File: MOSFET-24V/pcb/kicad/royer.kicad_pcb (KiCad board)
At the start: 2 copper layers, 53.3 x 73.7 mm, 25 parts, among them J1 9-24V, J2 COIL, Q1 IRFB4410, Q2 IRFD110, Q3 IRFD110, Q4 IRFB4410

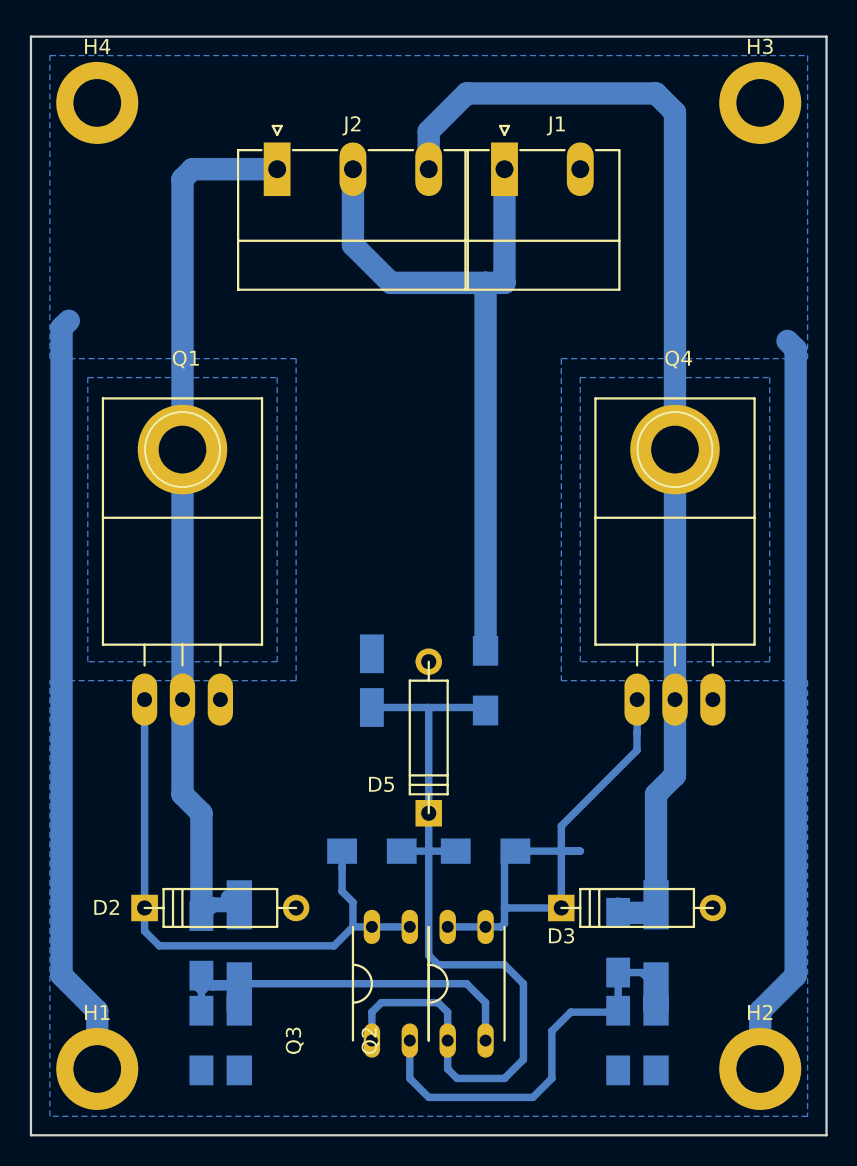
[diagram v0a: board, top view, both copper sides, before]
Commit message: compacting PCB
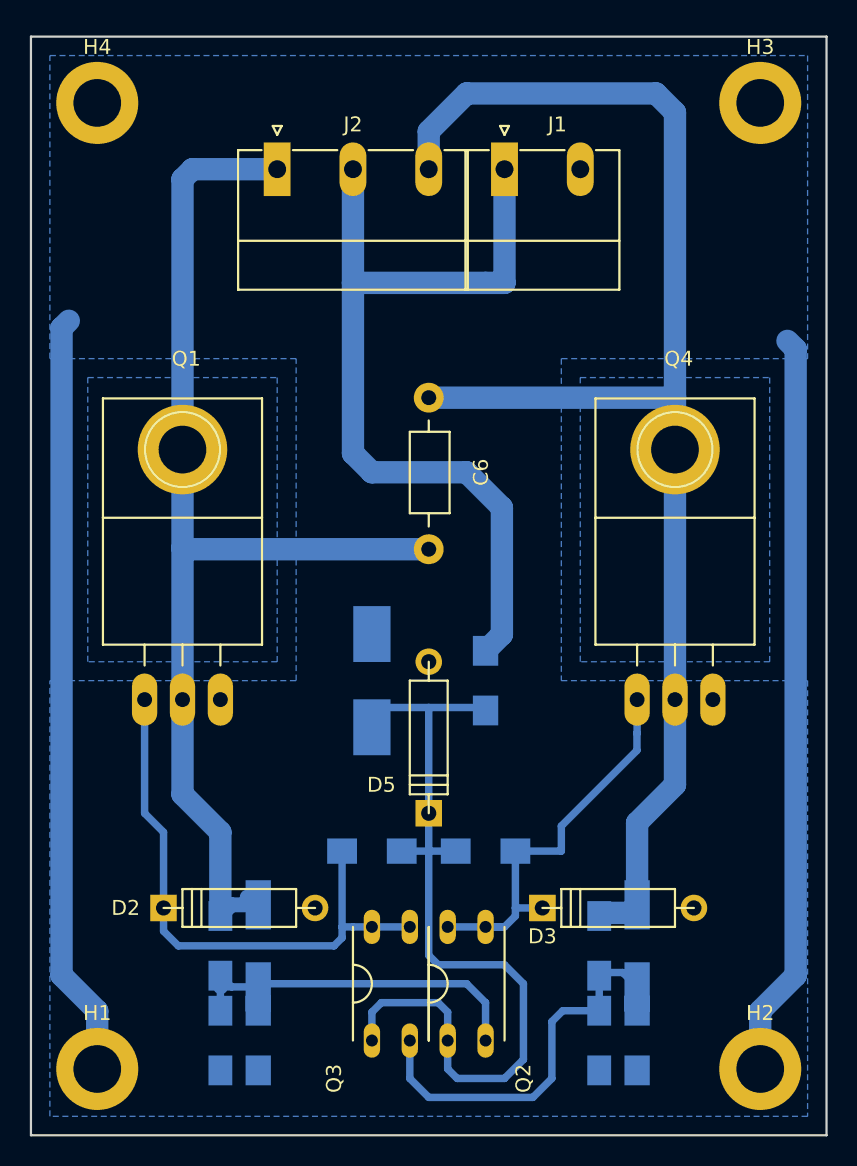
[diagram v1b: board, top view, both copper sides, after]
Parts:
- added C6: 1uF, Choke_Axial_ThroughHole:Choke_Horizontal_RM10mm, F.Cu at (177.8, 99.1)
- C5: value 1uF -> 4.7uF; footprint Capacitors_SMD:c_elec_4x5.8 -> Capacitors_Tantalum_SMD:Tantalum_Case-C_EIA-6032-28_Hand
- moved C4 1.29 mm to (189.2, 130.8)
- moved C1 1.27 mm to (163.8, 130.8)
- moved C2 1.27 mm to (163.8, 137.2)
- moved C3 1.27 mm to (189.2, 137.2)
- moved D1 1.27 mm to (166.4, 130.8)
- moved D3 1.27 mm to (190.5, 128.3)
- moved R1 1.27 mm to (166.4, 137.2)
- moved D2 1.27 mm to (165.1, 128.3)
- moved D4 1.27 mm to (191.8, 130.8)
- moved R5 1.27 mm to (191.8, 137.2)
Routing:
- net /C1: track 59.6 -> 77.4 mm
- net /C2: track 78.1 -> 94.4 mm
- net /24V: track 48.6 -> 58.4 mm
- net /G2: track 34.3 -> 27.4 mm
- net /D1: track 28.2 -> 24.4 mm
- net /D2: track 29.9 -> 29.1 mm
- net /G1: track 41.3 -> 40.7 mm

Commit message: compacting PCB
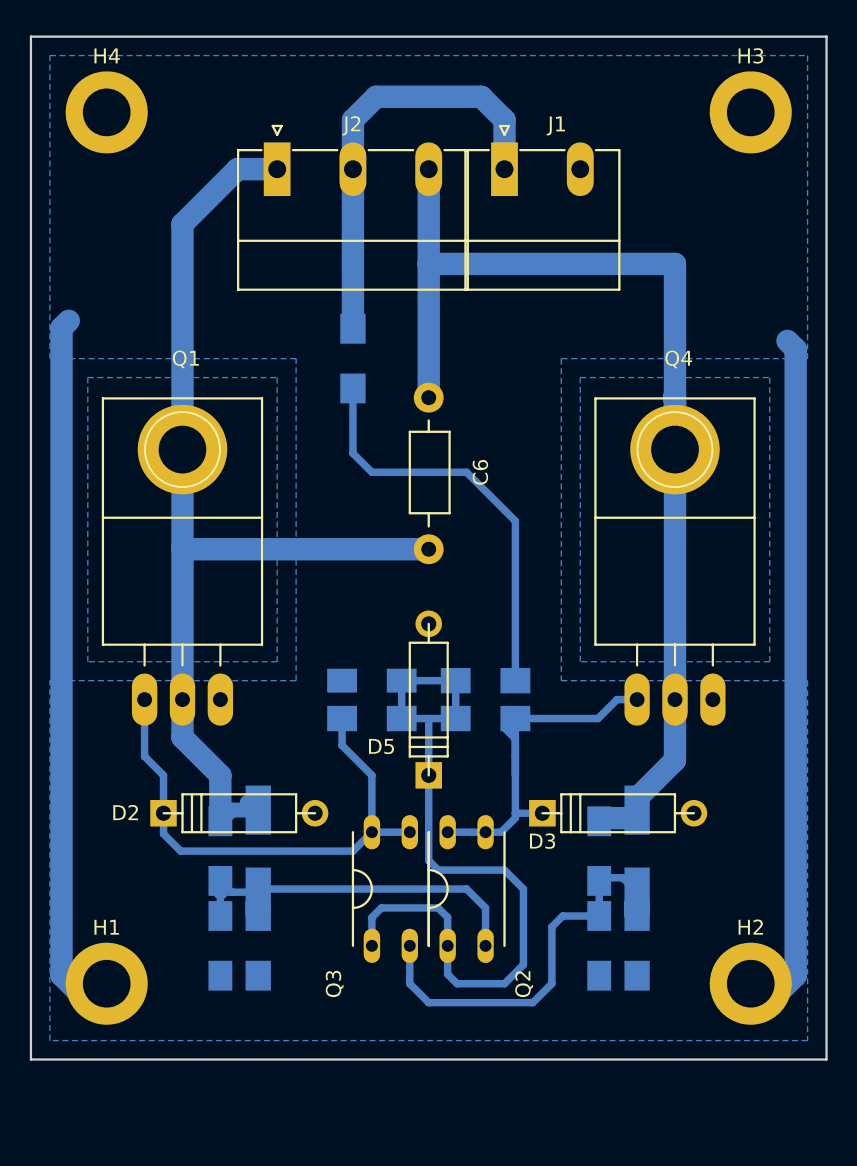
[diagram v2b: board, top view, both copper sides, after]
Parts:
- removed R7: 1.5k, Resistors_SMD:R_1206_HandSoldering
- added R2: 47k, Resistors_SMD:R_1206_HandSoldering, B.Cu at (181.6, 115.6)
- added R6: 1k, Resistors_SMD:R_1206_HandSoldering, B.Cu at (172.7, 91.4)
- C5: value 4.7uF -> 47nF; footprint Capacitors_Tantalum_SMD:Tantalum_Case-C_EIA-6032-28_Hand -> Capacitors_SMD:C_1206_HandSoldering
- R4: value 47k -> 33k
- R5: value 33k -> 1k
- moved R5 26.2 mm to (181.6, 113.0), turned to 180 degrees
- moved R4 18.9 mm to (191.8, 130.8), turned to 270 degrees
- moved R3 11.7 mm to (174.0, 115.6), turned to 180 degrees
- moved C1 6.35 mm to (163.8, 124.5)
- moved C4 6.35 mm to (189.2, 124.5)
- moved D1 6.35 mm to (166.4, 124.5)
- moved D2 6.35 mm to (165.1, 121.9)
- moved D3 6.35 mm to (190.5, 121.9)
- moved D4 6.35 mm to (191.8, 124.5)
- moved C2 6.35 mm to (163.8, 130.8)
- moved C3 6.35 mm to (189.2, 130.8)
- moved Q2 6.35 mm to (179.1, 130.8)
- moved Q3 6.35 mm to (174.0, 130.8)
- moved R1 6.35 mm to (166.4, 130.8)
- moved H1 5.75 mm to (156.2, 133.3)
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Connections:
- R3 pad 2: /G2 -> /G1
- R4 pad 1: /9V -> /D2
- R4 pad 2: /G1 -> GND
- R5 pad 1: /D2 -> Net-(R5-Pad1)
- R5 pad 2: GND -> /9V
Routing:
- net /24V: track 58.4 -> 28.8 mm
- net Net-(R5-Pad1): track 0.00 -> 27.8 mm
- net /C2: track 94.4 -> 76.2 mm
- net /C1: track 77.4 -> 69.3 mm
- net GND: track 101.4 -> 93.6 mm
- net /9V: track 57.3 -> 51.3 mm
- net /G1: track 40.7 -> 35.5 mm
- net /G2: track 27.4 -> 25.6 mm
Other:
- board size 53.3 x 73.7 mm -> 53.3 x 68.6 mm

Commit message: enlarging holes 3.2->3.5 mm# Please enter the commit message for your changes. Lines starting
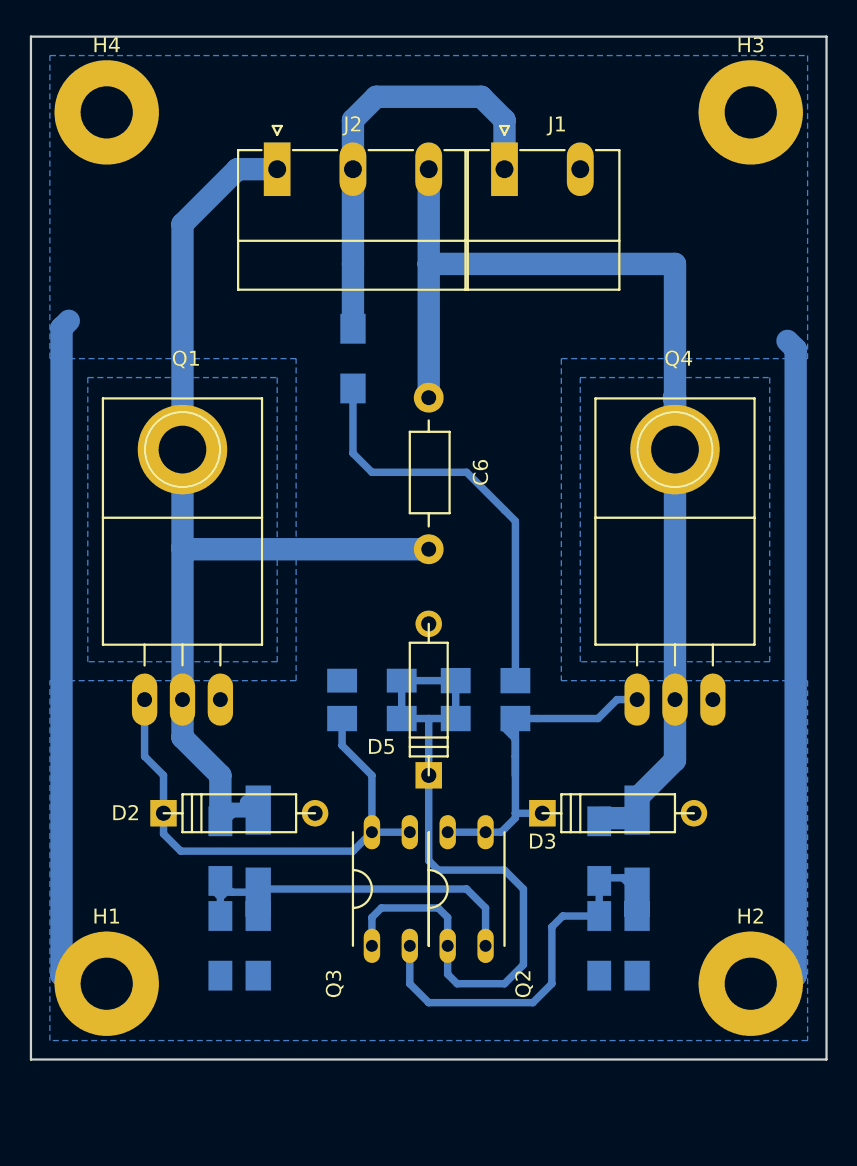
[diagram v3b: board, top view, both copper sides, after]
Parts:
- H1, H2, H3, H4: value 3.2mm -> 3.5mm; footprint Mounting_Holes:MountingHole_3.2mm_M3_ISO14580_Pad -> Mounting_Holes:MountingHole_3.5mm_Pad
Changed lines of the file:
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@@
     )
-  )
-  (module Mounting_Holes:MountingHole_3.2mm_M3_ISO14580_Pad (layer F.Cu)
-    (at 156.21 133.35)
-    (descr "Mounting Hole 3.2mm, M3, ISO14580")
-    (tags "mounting hole 3.2mm m3 iso14580")
-    (fp_text reference H1 (at 0 -3.75) (layer F.SilkS)
-      (effects (font (size 1 1) (thickness 0.15)))
-    )
-    (fp_text value 3.2mm (at 0 3.75) (layer F.Fab)
-      (effects (font (size 1 1) (thickness 0.15)))
-    )
-    (fp_circle (center 0 0) (end 2.75 0) (layer Cmts.User) (width 0.15))
-    (fp_circle (center 0 0) (end 3 0) (layer F.CrtYd) (width 0.05))
-    (pad 1 thru_hole circle (at 0 0) (size 5.5 5.5) (drill 3.2) (layers *.Cu *.Mask)
-      (net 1 GND))
-  )
-  (module Mounting_Holes:MountingHole_3.2mm_M3_ISO14580_Pad (layer F.Cu)
-    (at 199.39 133.35)
-    (descr "Mounting Hole 3.2mm, M3, ISO14580")
-    (tags "mounting hole 3.2mm m3 iso14580")
-    (fp_text reference H2 (at 0 -3.75) (layer F.SilkS)
-      (effects (font (size 1 1) (thickness 0.15)))
-    )
-    (fp_text value 3.2mm (at 0 3.75) (layer F.Fab)
-      (effects (font (size 1 1) (thickness 0.15)))
-    )
-    (fp_circle (center 0 0) (end 2.75 0) (layer Cmts.User) (width 0.15))
-    (fp_circle (center 0 0) (end 3 0) (layer F.CrtYd) (width 0.05))
-    (pad 1 thru_hole circle (at 0 0) (size 5.5 5.5) (drill 3.2) (layers *.Cu *.Mask)
-      (net 1 GND))
   )
   (module TO-220:TO-220_Neutral123_Horizontal_LargePads (layer F.Cu)
@@
     )
   )
-  (module Mounting_Holes:MountingHole_3.2mm_M3_ISO14580_Pad (layer F.Cu)
-    (at 199.39 74.93)
-    (descr "Mounting Hole 3.2mm, M3, ISO14580")
-    (tags "mounting hole 3.2mm m3 iso14580")
-    (fp_text reference H3 (at 0 -3.75) (layer F.SilkS)
-      (effects (font (size 1 1) (thickness 0.15)))
-    )
-    (fp_text value 3.2mm (at 0 3.75) (layer F.Fab)
-      (effects (font (size 1 1) (thickness 0.15)))
-    )
-    (fp_circle (center 0 0) (end 2.75 0) (layer Cmts.User) (width 0.15))
-    (fp_circle (center 0 0) (end 3 0) (layer F.CrtYd) (width 0.05))
-    (pad 1 thru_hole circle (at 0 0) (size 5.5 5.5) (drill 3.2) (layers *.Cu *.Mask)
-      (net 1 GND))
-  )
-  (module Mounting_Holes:MountingHole_3.2mm_M3_ISO14580_Pad (layer F.Cu)
-    (at 156.21 74.93)
-    (descr "Mounting Hole 3.2mm, M3, ISO14580")
-    (tags "mounting hole 3.2mm m3 iso14580")
-    (fp_text reference H4 (at 0 -3.75) (layer F.SilkS)
-      (effects (font (size 1 1) (thickness 0.15)))
-    )
-    (fp_text value 3.2mm (at 0 3.75) (layer F.Fab)
-      (effects (font (size 1 1) (thickness 0.15)))
-    )
-    (fp_circle (center 0 0) (end 2.75 0) (layer Cmts.User) (width 0.15))
-    (fp_circle (center 0 0) (end 3 0) (layer F.CrtYd) (width 0.05))
-    (pad 1 thru_hole circle (at 0 0) (size 5.5 5.5) (drill 3.2) (layers *.Cu *.Mask)
-      (net 1 GND))
-  )
   (module Choke_Axial_ThroughHole:Choke_Horizontal_RM10mm (layer F.Cu)
     (at 177.8 99.06 270)
@@
     )
   )
+  (module Mounting_Holes:MountingHole_3.5mm_Pad (layer F.Cu)
+    (at 156.21 133.35)
+    (descr "Mounting Hole 3.5mm")
+    (tags "mounting hole 3.5mm")
+    (fp_text reference H1 (at 0 -4.5) (layer F.SilkS)
+      (effects (font (size 1 1) (thickness 0.15)))
+    )
+    (fp_text value 3.5mm (at 0 4.5) (layer F.Fab)
+      (effects (font (size 1 1) (thickness 0.15)))
+    )
+    (fp_circle (center 0 0) (end 3.5 0) (layer Cmts.User) (width 0.15))
+    (fp_circle (center 0 0) (end 3.75 0) (layer F.CrtYd) (width 0.05))
+    (pad 1 thru_hole circle (at 0 0) (size 7 7) (drill 3.5) (layers *.Cu *.Mask)
+      (net 1 GND))
+  )
+  (module Mounting_Holes:MountingHole_3.5mm_Pad (layer F.Cu)
+    (at 199.39 133.35)
+    (descr "Mounting Hole 3.5mm")
+    (tags "mounting hole 3.5mm")
+    (fp_text reference H2 (at 0 -4.5) (layer F.SilkS)
+      (effects (font (size 1 1) (thickness 0.15)))
+    )
+    (fp_text value 3.5mm (at 0 4.5) (layer F.Fab)
+      (effects (font (size 1 1) (thickness 0.15)))
+    )
+    (fp_circle (center 0 0) (end 3.5 0) (layer Cmts.User) (width 0.15))
+    (fp_circle (center 0 0) (end 3.75 0) (layer F.CrtYd) (width 0.05))
+    (pad 1 thru_hole circle (at 0 0) (size 7 7) (drill 3.5) (layers *.Cu *.Mask)
+      (net 1 GND))
+  )
+  (module Mounting_Holes:MountingHole_3.5mm_Pad (layer F.Cu)
+    (at 199.39 74.93)
+    (descr "Mounting Hole 3.5mm")
+    (tags "mounting hole 3.5mm")
+    (fp_text reference H3 (at 0 -4.5) (layer F.SilkS)
+      (effects (font (size 1 1) (thickness 0.15)))
+    )
+    (fp_text value 3.5mm (at 0 4.5) (layer F.Fab)
+      (effects (font (size 1 1) (thickness 0.15)))
+    )
+    (fp_circle (center 0 0) (end 3.5 0) (layer Cmts.User) (width 0.15))
+    (fp_circle (center 0 0) (end 3.75 0) (layer F.CrtYd) (width 0.05))
+    (pad 1 thru_hole circle (at 0 0) (size 7 7) (drill 3.5) (layers *.Cu *.Mask)
+      (net 1 GND))
+  )
+  (module Mounting_Holes:MountingHole_3.5mm_Pad (layer F.Cu)
+    (at 156.21 74.93)
+    (descr "Mounting Hole 3.5mm")
+    (tags "mounting hole 3.5mm")
+    (fp_text reference H4 (at 0 -4.5) (layer F.SilkS)
+      (effects (font (size 1 1) (thickness 0.15)))
+    )
+    (fp_text value 3.5mm (at 0 4.5) (layer F.Fab)
+      (effects (font (size 1 1) (thickness 0.15)))
+    )
+    (fp_circle (center 0 0) (end 3.5 0) (layer Cmts.User) (width 0.15))
+    (fp_circle (center 0 0) (end 3.75 0) (layer F.CrtYd) (width 0.05))
+    (pad 1 thru_hole circle (at 0 0) (size 7 7) (drill 3.5) (layers *.Cu *.Mask)
+      (net 1 GND))
+  )
   (dimension 58.42 (width 0.3) (layer Eco2.User)
